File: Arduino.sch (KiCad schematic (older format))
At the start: 21 parts

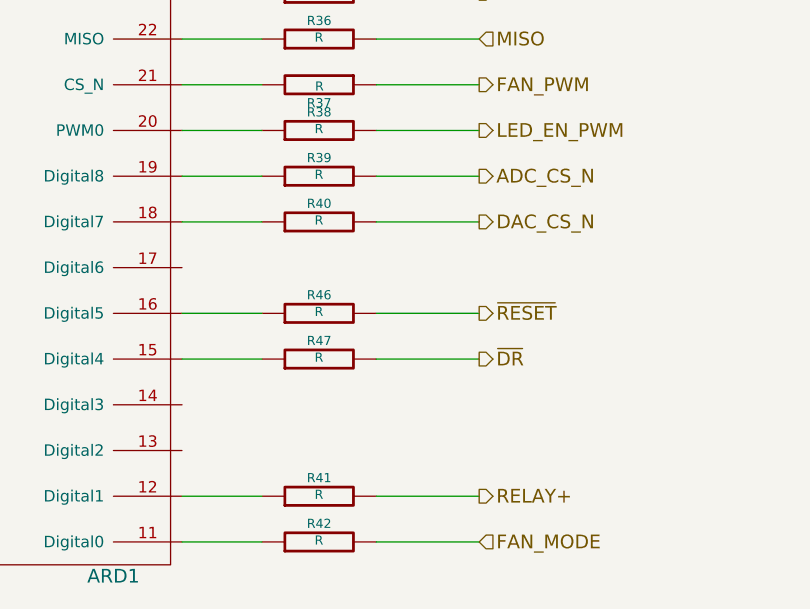
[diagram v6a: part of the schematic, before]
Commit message: Fan driver: assc/placement
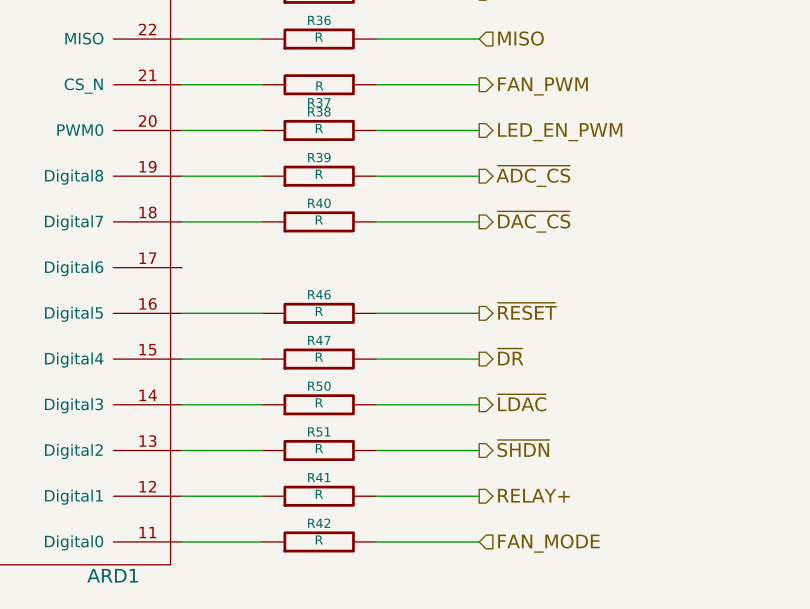
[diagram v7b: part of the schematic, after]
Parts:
- added R50, R51: R, ~, symbol R
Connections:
- net at ARD1.13 (Digital2): now also R51.1
- net at ARD1.14 (Digital3): now also R50.1
- net ADC_CS_N renamed ~ADC_CS
- net DAC_CS_N renamed ~DAC_CS
- new net ~LDAC: R50.2
- new net ~SHDN: R51.2
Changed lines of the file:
@@
 $Descr A4 11693 8268
 encoding utf-8
-Sheet 7 9
+Sheet 9 9
 Title ""
-Date "22 feb 2014"
+Date "23 feb 2014"
 Rev ""
 Comp ""
@@
 SCLK
 Text HLabel 6350 4000 2    60   Output ~ 0
-DAC_CS_N
+~DAC_CS
 Text HLabel 6350 3400 2    60   Output ~ 0
 FAN_PWM
@@
 	5900 5200 6350 5200
 $Comp
-L GND #PWR43
+L GND #PWR060
 U 1 1 52F88224
 P 8000 4800
-F 0 "#PWR43" H 8000 4800 30  0001 C CNN
+F 0 "#PWR060" H 8000 4800 30  0001 C CNN
 F 1 "GND" H 8000 4730 30  0001 C CNN
 F 2 "" H 8000 4800 60  0000 C CNN
@@
 	5050 3800 5400 3800
 Text HLabel 6350 3800 2    60   Output ~ 0
-ADC_CS_N
+~ADC_CS
 Wire Wire Line
 	6350 3800 5900 3800
@@
 	2900 3450 3100 3450
 $Comp
-L +12P #PWR40
+L +12P #PWR061
 U 1 1 52F7F246
 P 1250 3200
-F 0 "#PWR40" H 1250 3170 30  0001 C CNN
+F 0 "#PWR061" H 1250 3170 30  0001 C CNN
 F 1 "+12P" H 1250 3300 30  0000 C CNN
 F 2 "" H 1250 3200 60  0000 C CNN
@@
 	2900 3250 3100 3250
 $Comp
-L GND #PWR41
+L GND #PWR062
 U 1 1 5302C5E6
 P 1900 3350
-F 0 "#PWR41" H 1900 3350 30  0001 C CNN
+F 0 "#PWR062" H 1900 3350 30  0001 C CNN
 F 1 "GND" H 1900 3280 30  0001 C CNN
 F 2 "" H 1900 3350 60  0000 C CNN
@@
 Connection ~ 1900 3250
 $Comp
-L +5V #PWR42
+L +5V #PWR063
 U 1 1 5302C682
 P 2050 2600
-F 0 "#PWR42" H 2050 2690 20  0001 C CNN
+F 0 "#PWR063" H 2050 2690 20  0001 C CNN
 F 1 "+5V" H 2050 2690 30  0000 C CNN
 F 2 "" H 2050 2600 60  0000 C CNN
@@
 	1    0    0    -1
 $EndComp
+$Comp
+L R R50
+U 1 1 53095B58
+P 5650 4800
+F 0 "R50" V 5730 4800 40  0000 C CNN
+F 1 "R" V 5657 4801 40  0000 C CNN
+F 2 "~" V 5580 4800 30  0000 C CNN
+F 3 "~" H 5650 4800 30  0000 C CNN
+	1    5650 4800
+	0    -1   -1   0
+$EndComp
+Wire Wire Line
+	5400 4800 5050 4800
+Wire Wire Line
+	5900 4800 6350 4800
+$Comp
+L R R51
+U 1 1 53095B60
+P 5650 5000
+F 0 "R51" V 5730 5000 40  0000 C CNN
+F 1 "R" V 5657 5001 40  0000 C CNN
+F 2 "~" V 5580 5000 30  0000 C CNN
+F 3 "~" H 5650 5000 30  0000 C CNN
+	1    5650 5000
+	0    -1   -1   0
+$EndComp
+Wire Wire Line
+	5400 5000 5050 5000
+Wire Wire Line
+	5900 5000 6350 5000
+Text HLabel 6350 4800 2    60   Output ~ 0
+~LDAC
+Text HLabel 6350 5000 2    60   Output ~ 0
+~SHDN
 $EndSCHEMATC
